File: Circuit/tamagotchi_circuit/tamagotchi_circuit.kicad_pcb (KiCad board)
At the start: 2 copper layers, 114.3 x 42.9 mm, 5 parts

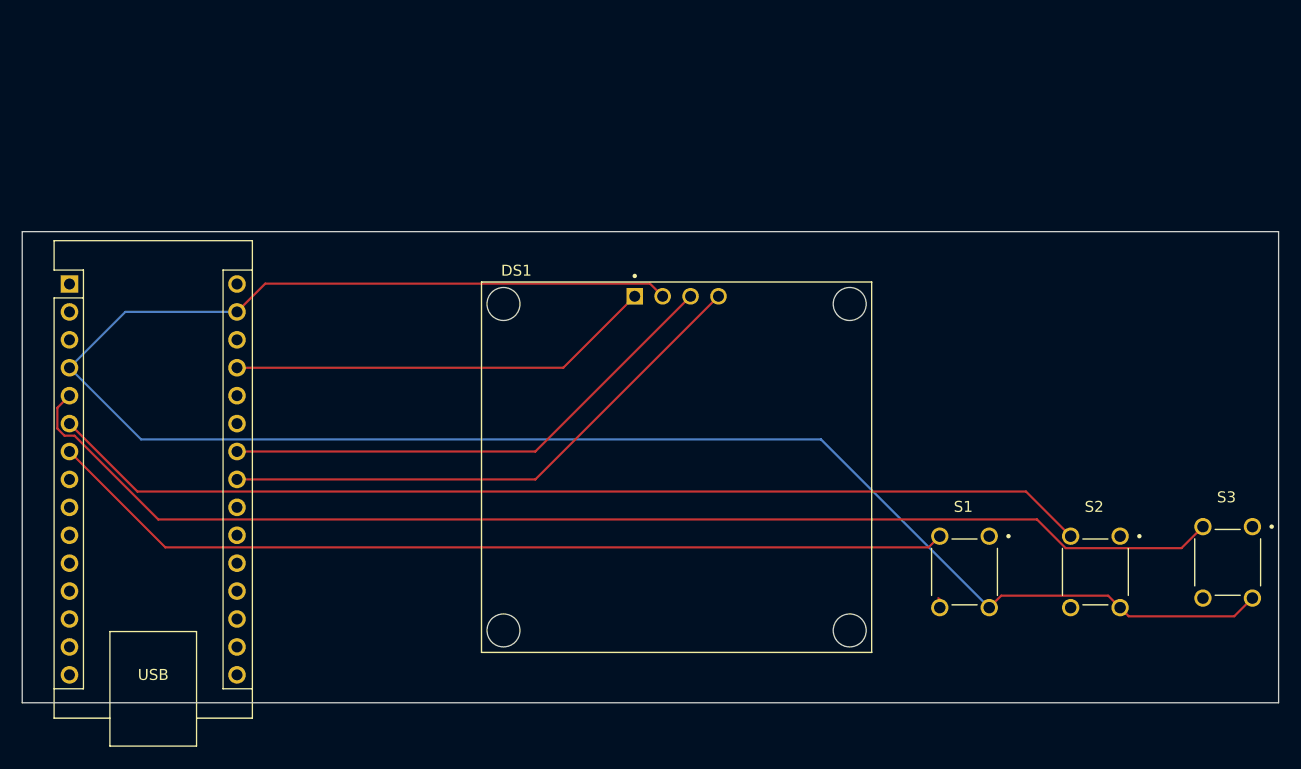
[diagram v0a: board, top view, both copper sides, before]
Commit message: Update circuit schematic footprints, add new images, and enhance documentation
- Updated footprints for components in the tamagotchi circuit schematic.
- Added new images including Front.PNG, QRCODE.png, QR_TRANSPARENT.png, arduino_transparent.png, screen_Front_transparent.png, and shell.png.
- Updated the README.md to include a section for the shell image.
- Added new zine files: Tamagotchi Zine.pdf and Tamagotchi Zine.png.
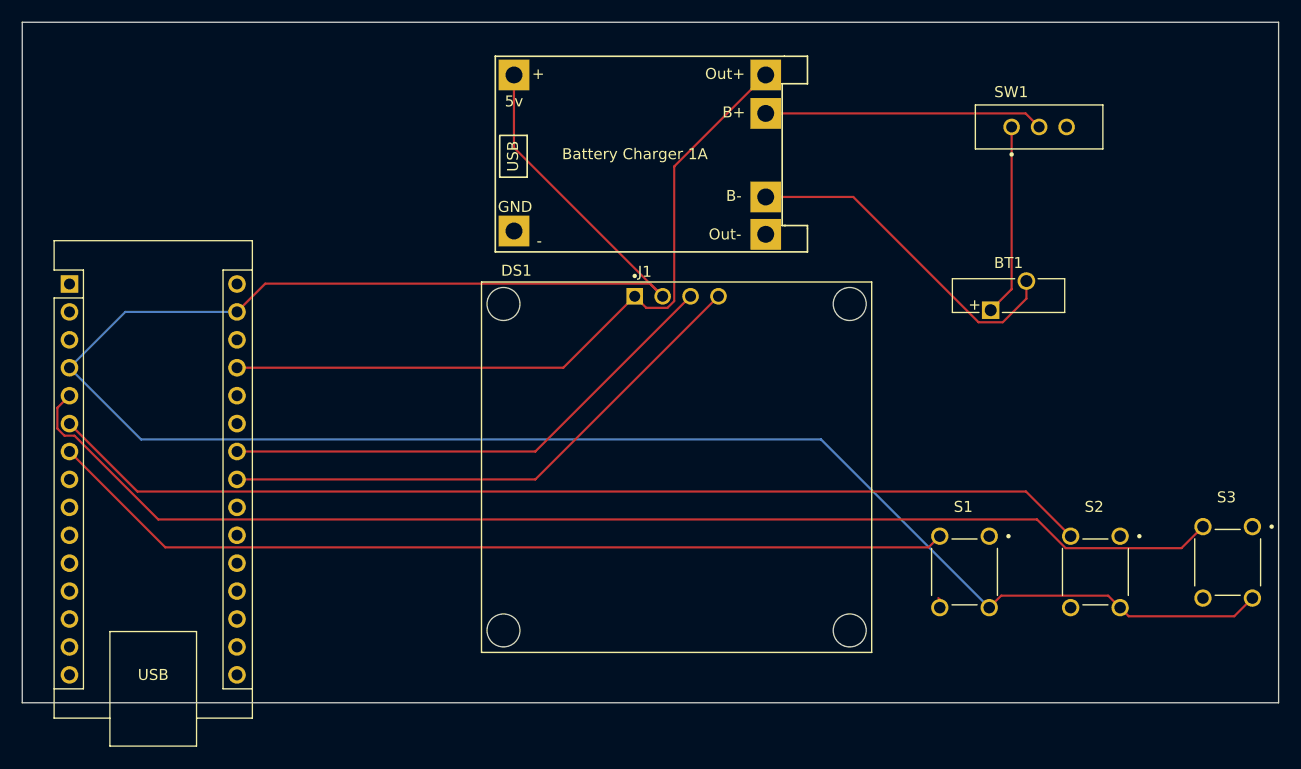
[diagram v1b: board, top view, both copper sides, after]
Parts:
- added BT1: Battery, Battery:Battery_Panasonic_CR1025-VSK_Vertical_CircularHoles, F.Cu at (226.2, 83.3)
- added J1: Conn_01x06, TP4056-18650-master:TP4056-18650, F.Cu at (181.2, 60.2)
- added SW1: SW_SPDT, EG1218:SW_EG1218, F.Cu at (230.6, 66.7)
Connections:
- net Net-(A1-+5V) renamed /OUT+
- net Net-(DS1-GND) renamed /In+
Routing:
- net /BAT-: track 0.00 -> 30.9 mm
- net /OUT+: track 38.9 -> 67.2 mm
- net /In+: track 176.2 -> 201.9 mm
- net /BAT+: track 0.00 -> 25.4 mm
- net Net-(BT1-+): track 0.00 -> 17.5 mm
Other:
- board size 114.3 x 42.9 mm -> 114.3 x 61.9 mm
